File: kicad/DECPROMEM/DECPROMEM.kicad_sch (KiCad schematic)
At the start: 138 parts, among them J10 BDAL08, J100 A15, J101 A16, J102 A17, J103 A18, J104 A19, J105 A20, J106 A21, J107 +5V, J11 BDAL09, J12 BDAL10, J13 BDAL11, J14 BDAL12, J15 BDAL13, J16 BDAL14, J17 BDAL15, J18 BDAL16, J19 BDAL17, J2 BDAL00, J20 BDAL18, J21 BDAL19, J22 BDAL20, J23 BDAL21, J24 BRPLYL, J25 BMDENL, J26 BWRITEL, J27 BWLBL, J28 BWHBL, J29 BSDENL, J3 BDAL01, J30 SSnL, J31 BDSL, J32 BASL, J33 BIOSELL, J34 BDCOKH, J35 GND, J36 GND, J37 GND, J38 DAH00, J39 DAH01, J4 BDAL02, J40 DAH02, J41 DAH03, J42 DAH04, J43 DAH05, J44 DAH06, J45 DAH07, J46 DAH08, J47 DAH09, J48 DAH10, J49 DAH11, J5 BDAL03, J50 DAH12, J51 DAH13, J52 DAH14, J53 DAH15, J54 DAH16, J55 DAH17, J56 DAH18, J57 DAH19, J58 DAH20, J59 DAH21, J6 BDAL04, J60 JTAG, J61 ASL, J62 MDENL, J63 SDENL, J64 MOEL, J65 MWEL, J66 MCELOWH, J67 MLEL, J68 MCEHIGHL, J69 MHEL, J7 BDAL05, J70 BUSDIR, J71 BUSOE, J72 CLK, J73 MA15, J74 MA16, J75 MA17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

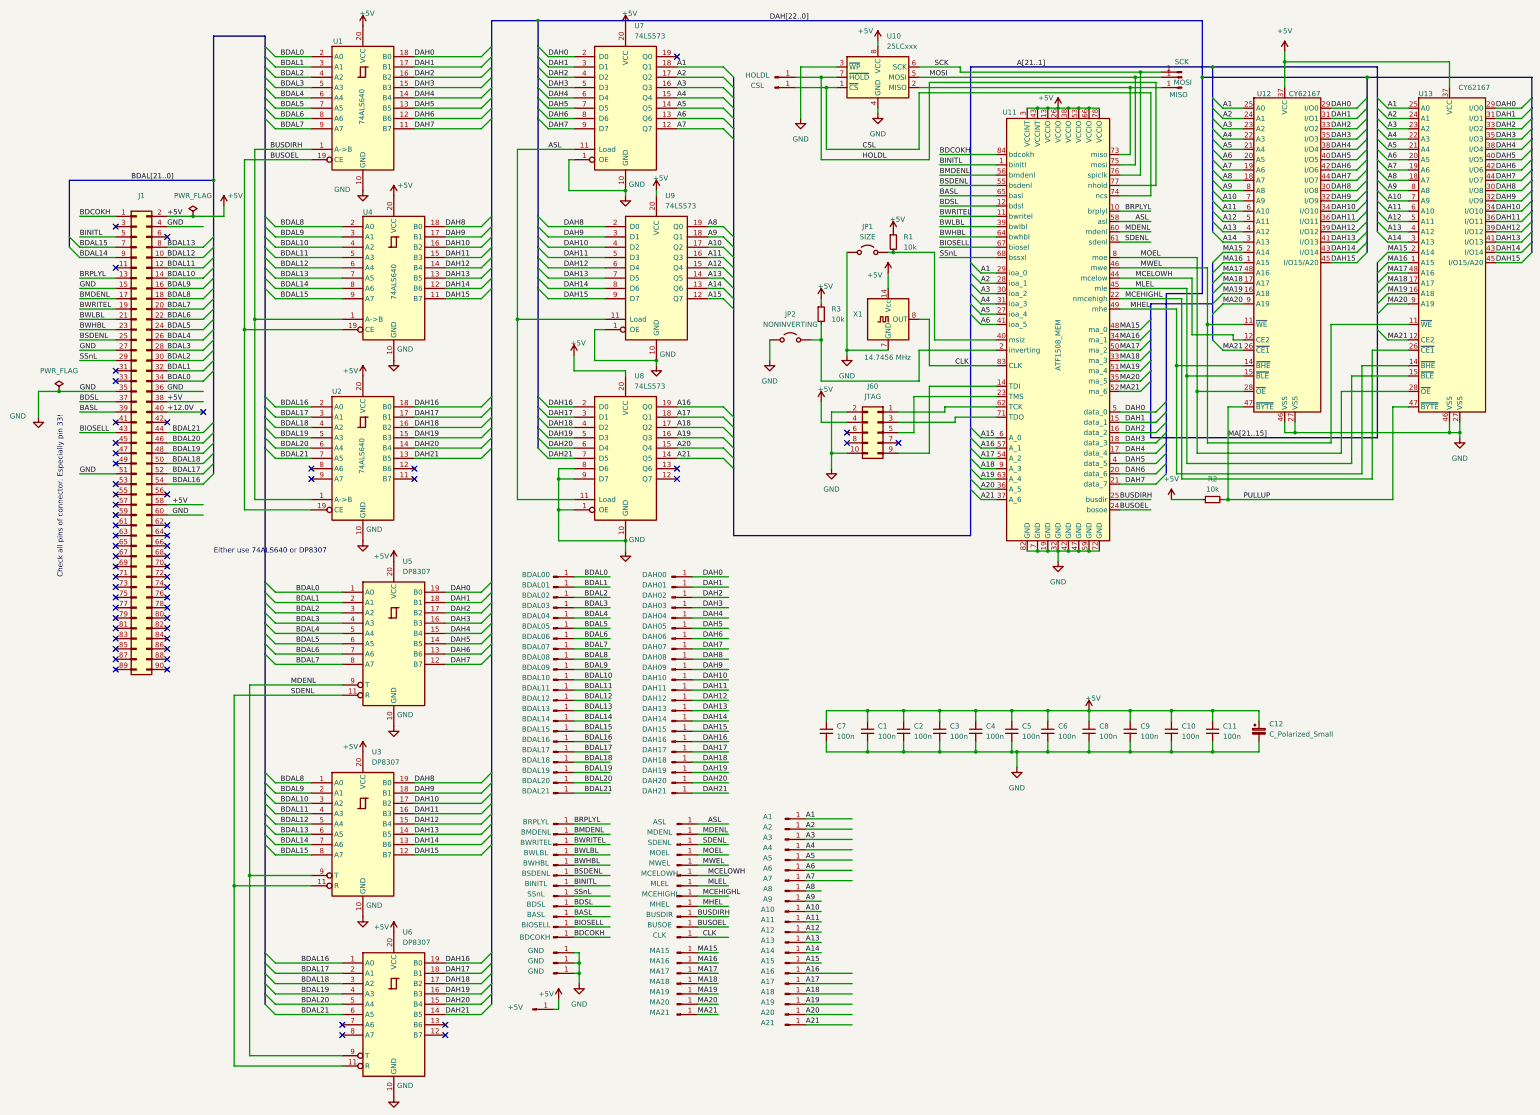
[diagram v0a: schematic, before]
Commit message: Fixing A - B port mixup on trsnceivers.
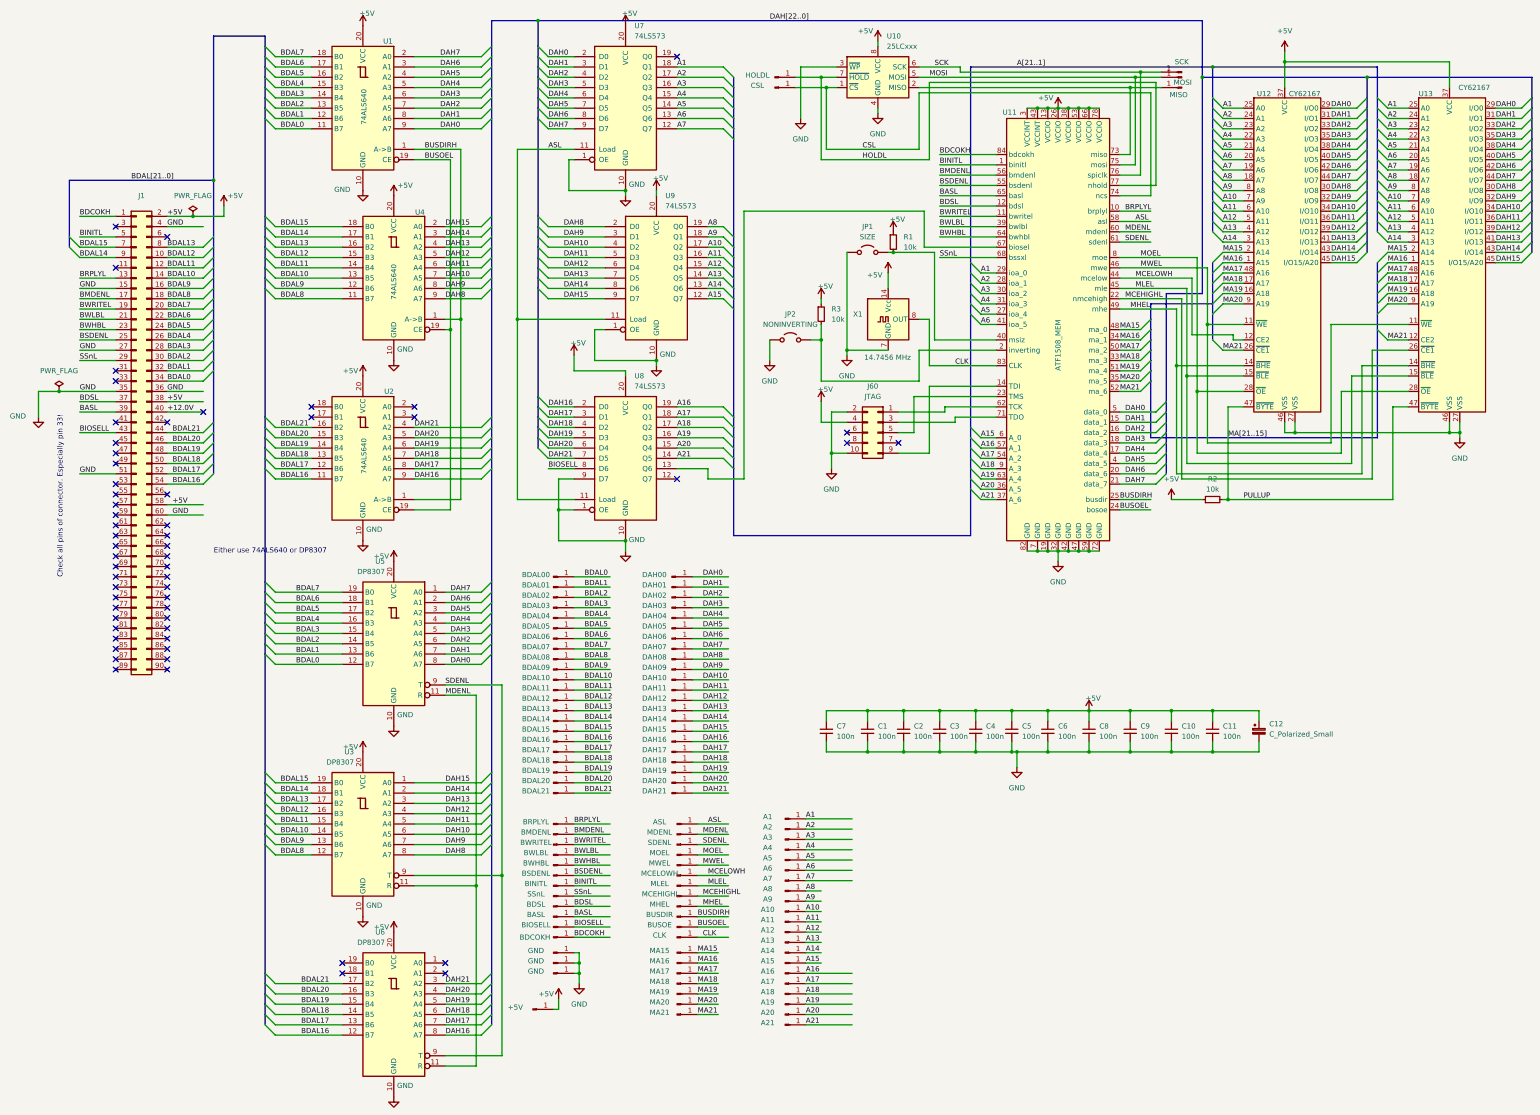
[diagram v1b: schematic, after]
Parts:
- X1: footprint Package_DIP:DIP-14_W7.62mm -> Oscillator:Oscillator_DIP-14
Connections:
- net BDAL0: now also U1.11 (B7), U5.12 (B7); no longer U1.2 (A0), U5.1 (A0)
- net BDAL1: now also U1.12 (B6), U5.13 (B6); no longer U1.3 (A1), U5.2 (A1)
- net BDAL10: now also U3.14 (B5), U4.13 (B5); no longer U3.3 (A2), U4.4 (A2)
- net BDAL11: now also U3.15 (B4), U4.14 (B4); no longer U3.4 (A3), U4.5 (A3)
- net BDAL12: now also U3.16 (B3), U4.15 (B3); no longer U3.5 (A4), U4.6 (A4)
- net BDAL13: now also U3.17 (B2), U4.16 (B2); no longer U3.6 (A5), U4.7 (A5)
- net BDAL14: now also U3.18 (B1), U4.17 (B1); no longer U3.7 (A6), U4.8 (A6)
- net BDAL15: now also U3.19 (B0), U4.18 (B0); no longer U3.8 (A7), U4.9 (A7)
- net BDAL16: now also U2.11 (B7), U6.12 (B7); no longer U2.2 (A0), U6.1 (A0)
- net BDAL17: now also U2.12 (B6), U6.13 (B6); no longer U2.3 (A1), U6.2 (A1)
- net BDAL18: now also U2.13 (B5), U6.14 (B5); no longer U2.4 (A2), U6.3 (A2)
- net BDAL19: now also U2.14 (B4), U6.15 (B4); no longer U2.5 (A3), U6.4 (A3)
- net BDAL2: now also U1.13 (B5), U5.14 (B5); no longer U1.4 (A2), U5.3 (A2)
- net BDAL20: now also U2.15 (B3), U6.16 (B3); no longer U2.6 (A4), U6.5 (A4)
- net BDAL21: now also U2.16 (B2), U6.17 (B2); no longer U2.7 (A5), U6.6 (A5)
- net BDAL3: now also U1.14 (B4), U5.15 (B4); no longer U1.5 (A3), U5.4 (A3)
- net BDAL4: now also U1.15 (B3), U5.16 (B3); no longer U1.6 (A4), U5.5 (A4)
- net BDAL5: now also U1.16 (B2), U5.17 (B2); no longer U1.7 (A5), U5.6 (A5)
- net BDAL6: now also U1.17 (B1), U5.18 (B1); no longer U1.8 (A6), U5.7 (A6)
- net BDAL7: now also U1.18 (B0), U5.19 (B0); no longer U1.9 (A7), U5.8 (A7)
- net BDAL8: now also U3.12 (B7), U4.11 (B7); no longer U3.1 (A0), U4.2 (A0)
- net BDAL9: now also U3.13 (B6), U4.12 (B6); no longer U3.2 (A1), U4.3 (A1)
- net BIOSELL: now also U8.8 (D6); no longer U11.67 (biosel)
- net DAH0: now also U1.9 (A7), U5.8 (A7); no longer U1.18 (B0), U5.19 (B0)
- net DAH1: now also U1.8 (A6), U5.7 (A6); no longer U1.17 (B1), U5.18 (B1)
- net DAH10: now also U3.6 (A5), U4.7 (A5); no longer U3.17 (B2), U4.16 (B2)
- net DAH11: now also U3.5 (A4), U4.6 (A4); no longer U3.16 (B3), U4.15 (B3)
- net DAH12: now also U3.4 (A3), U4.5 (A3); no longer U3.15 (B4), U4.14 (B4)
- net DAH13: now also U3.3 (A2), U4.4 (A2); no longer U3.14 (B5), U4.13 (B5)
- net DAH14: now also U3.2 (A1), U4.3 (A1); no longer U3.13 (B6), U4.12 (B6)
- net DAH15: now also U3.1 (A0), U4.2 (A0); no longer U3.12 (B7), U4.11 (B7)
- net DAH16: now also U2.9 (A7), U6.8 (A7); no longer U2.18 (B0), U6.19 (B0)
- net DAH17: now also U2.8 (A6), U6.7 (A6); no longer U2.17 (B1), U6.18 (B1)
- net DAH18: now also U2.7 (A5), U6.6 (A5); no longer U2.16 (B2), U6.17 (B2)
- net DAH19: now also U2.6 (A4), U6.5 (A4); no longer U2.15 (B3), U6.16 (B3)
- net DAH2: now also U1.7 (A5), U5.6 (A5); no longer U1.16 (B2), U5.17 (B2)
- net DAH20: now also U2.5 (A3), U6.4 (A3); no longer U2.14 (B4), U6.15 (B4)
- net DAH21: now also U2.4 (A2), U6.3 (A2); no longer U2.13 (B5), U6.14 (B5)
- net DAH3: now also U1.6 (A4), U5.5 (A4); no longer U1.15 (B3), U5.16 (B3)
- net DAH4: now also U1.5 (A3), U5.4 (A3); no longer U1.14 (B4), U5.15 (B4)
- net DAH5: now also U1.4 (A2), U5.3 (A2); no longer U1.13 (B5), U5.14 (B5)
- net DAH6: now also U1.3 (A1), U5.2 (A1); no longer U1.12 (B6), U5.13 (B6)
- net DAH7: now also U1.2 (A0), U5.1 (A0); no longer U1.11 (B7), U5.12 (B7)
- net DAH8: now also U3.8 (A7), U4.9 (A7); no longer U3.19 (B0), U4.18 (B0)
- net DAH9: now also U3.7 (A6), U4.8 (A6); no longer U3.18 (B1), U4.17 (B1)
- net GND: no longer U8.8 (D6)
- net MDENL: now also U3.11 (R), U5.11 (R), U6.11 (R); no longer U3.9 (T), U5.9 (T), U6.9 (T)
- net SDENL: now also U3.9 (T), U5.9 (T), U6.9 (T); no longer U3.11 (R), U5.11 (R), U6.11 (R)
- net at U8.13 (Q6): now also U11.67 (biosel)
- no-connect marks 60 -> 59

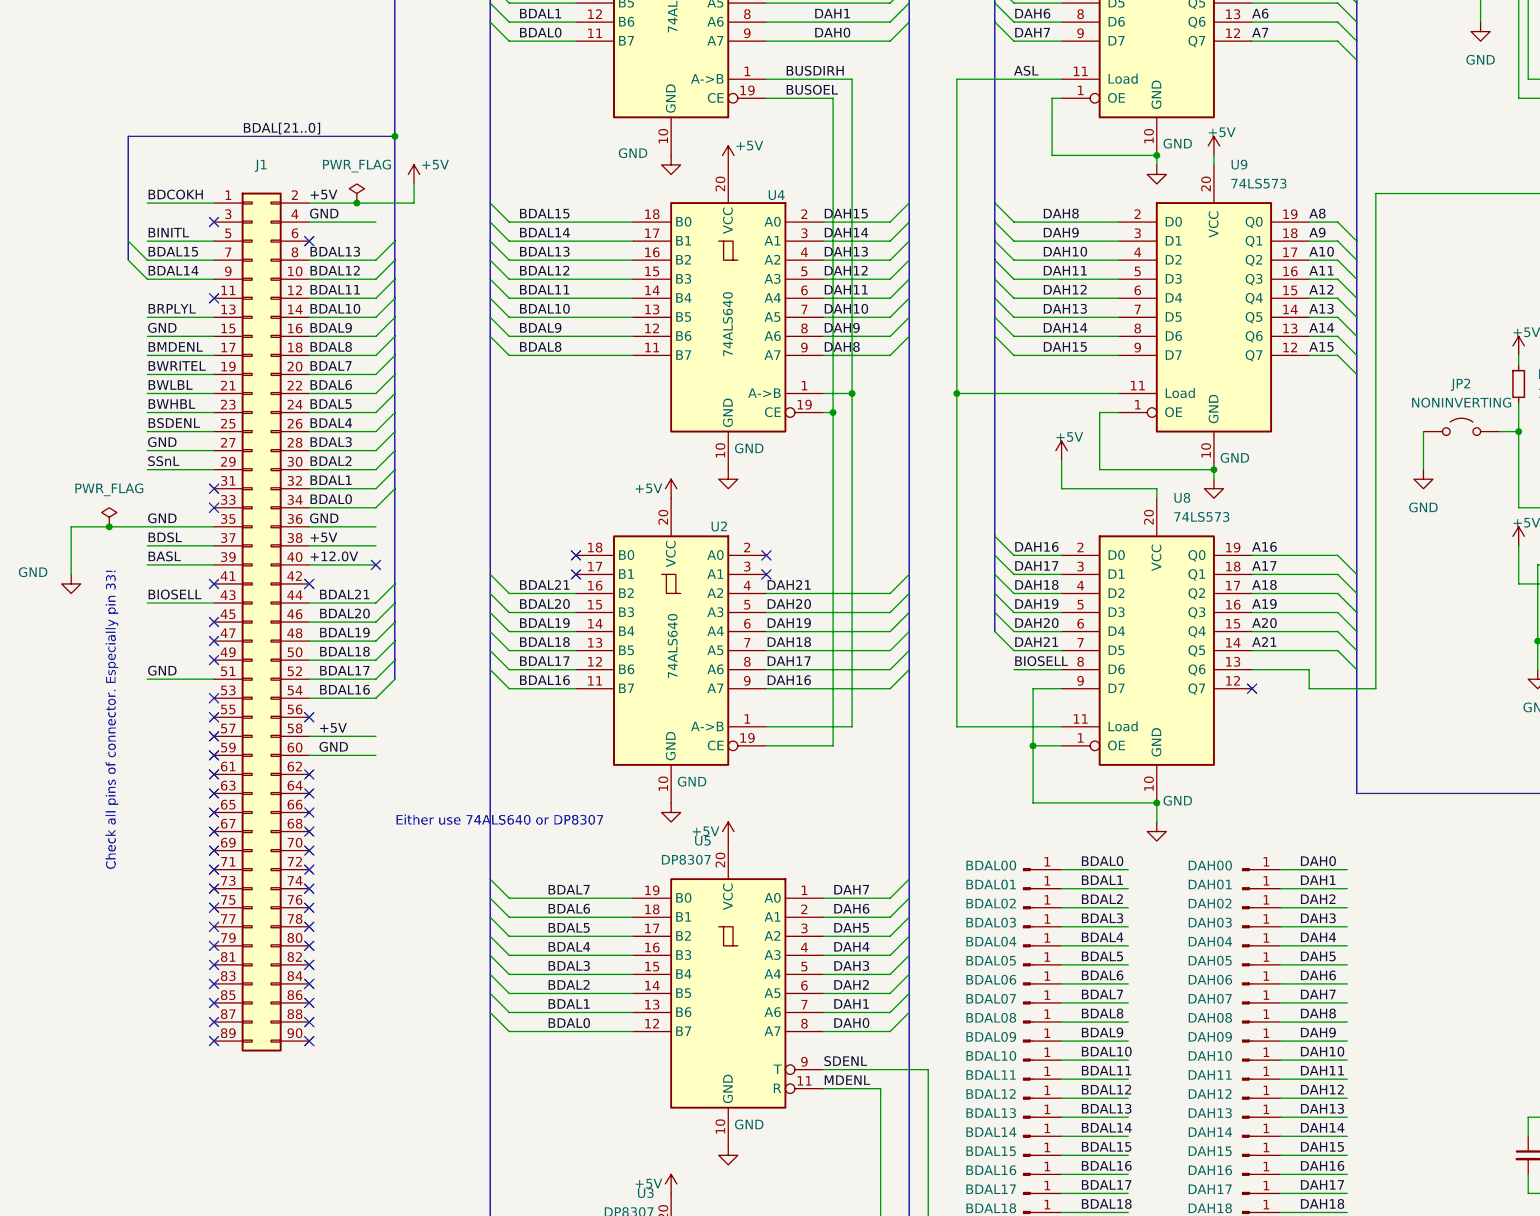
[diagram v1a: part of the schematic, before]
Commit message: Fixing texts in schematic
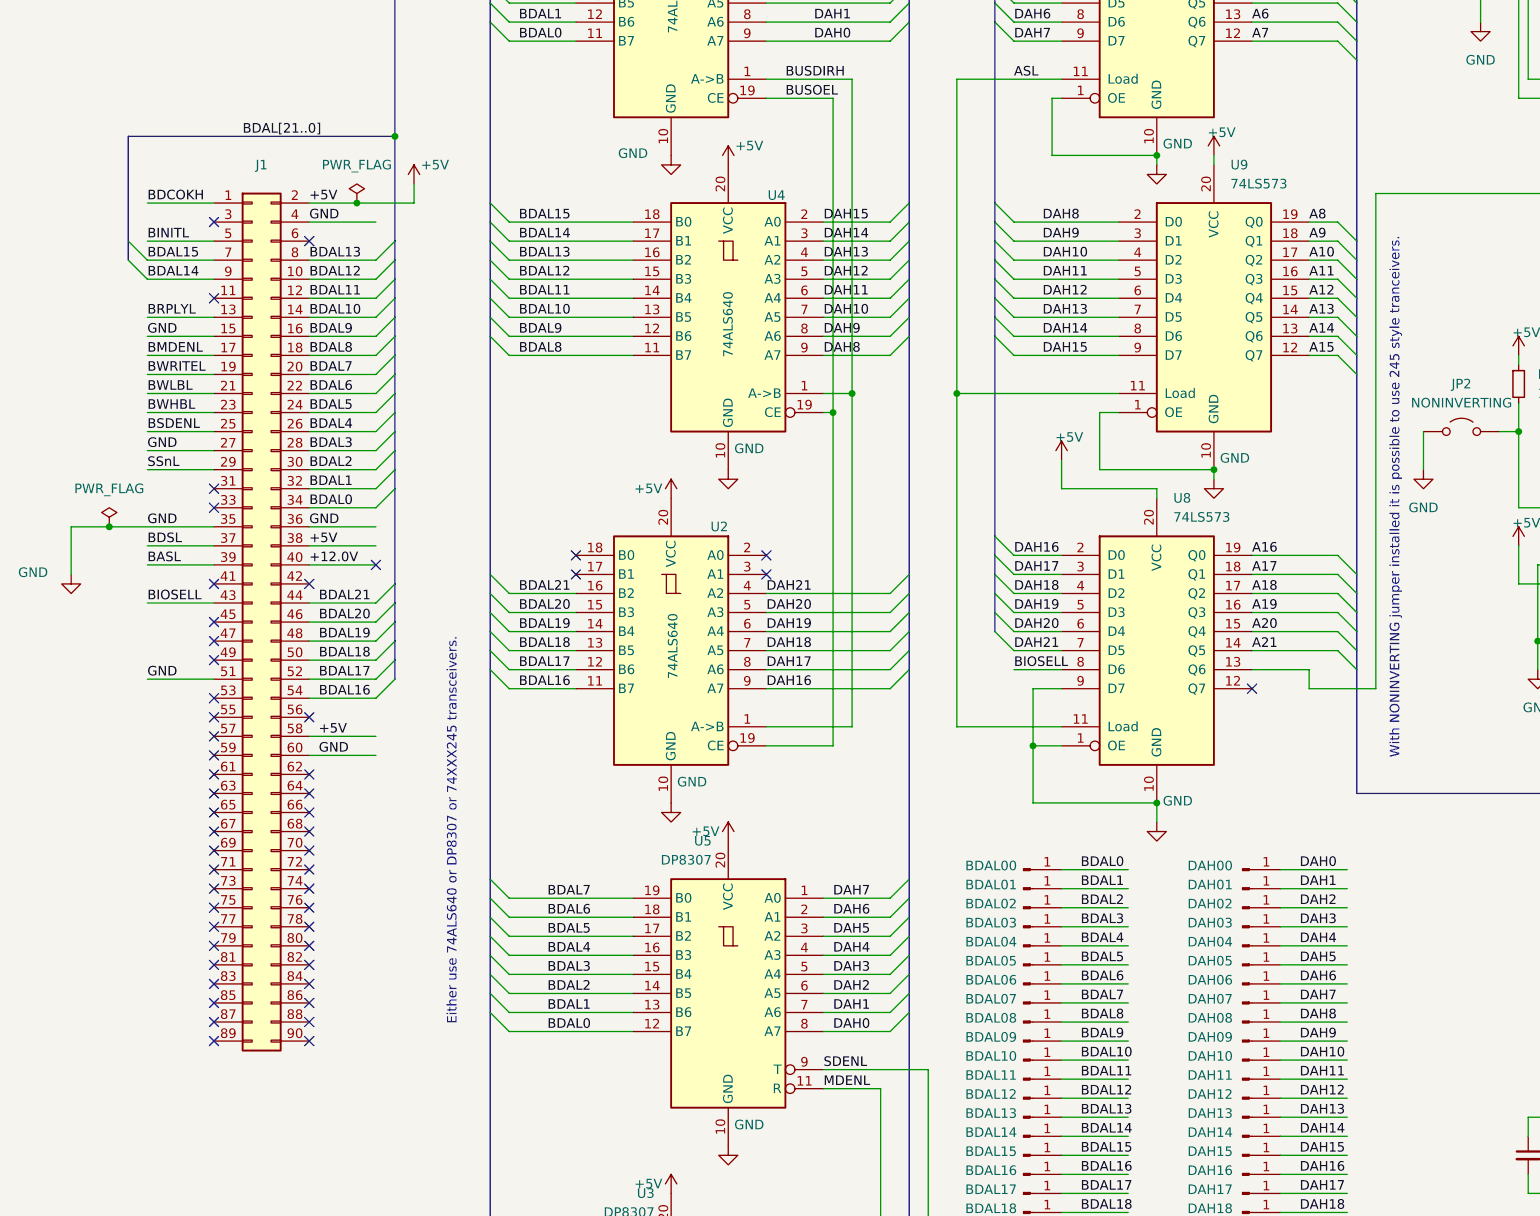
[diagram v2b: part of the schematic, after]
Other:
- note added: "Either use 74ALS640 or DP8307 or 74XXX245 transceivers."
- note added: "With NONINVERTING jumper installed it is possible to use 245 style tranceivers."
- note removed: "Check all pins of connector. Especially pin 33!"
- note removed: "Either use 74ALS640 or DP8307"
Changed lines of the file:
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@@
 		)
 	)
-	(text "Either use 74ALS640 or DP8307"
+	(text "Either use 74ALS640 or DP8307 or 74XXX245 transceivers."
 		(exclude_from_sim no)
-		(at 87.63 146.05 0)
+		(at 81.28 147.32 90)
 		(effects
 			(font
@@
 		)
 	)
-	(text "Check all pins of connector. Especially pin 33!"
+	(text "With NONINVERTING jumper installed it is possible to use 245 style tranceivers."
 		(exclude_from_sim no)
-		(at 35.814 132.588 90)
+		(at 207.01 102.87 90)
 		(effects
 			(font
